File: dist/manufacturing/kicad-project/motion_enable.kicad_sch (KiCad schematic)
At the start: 16 parts, among them Q14 MMBT5551LT1G, Q15 MMBT5551LT1G, U10 SN74LVC1G08DBVR, U11 SN74LVC1G08DBVR, U8 74LVC1G157GW,125, U9 74LVC1G157GW,125

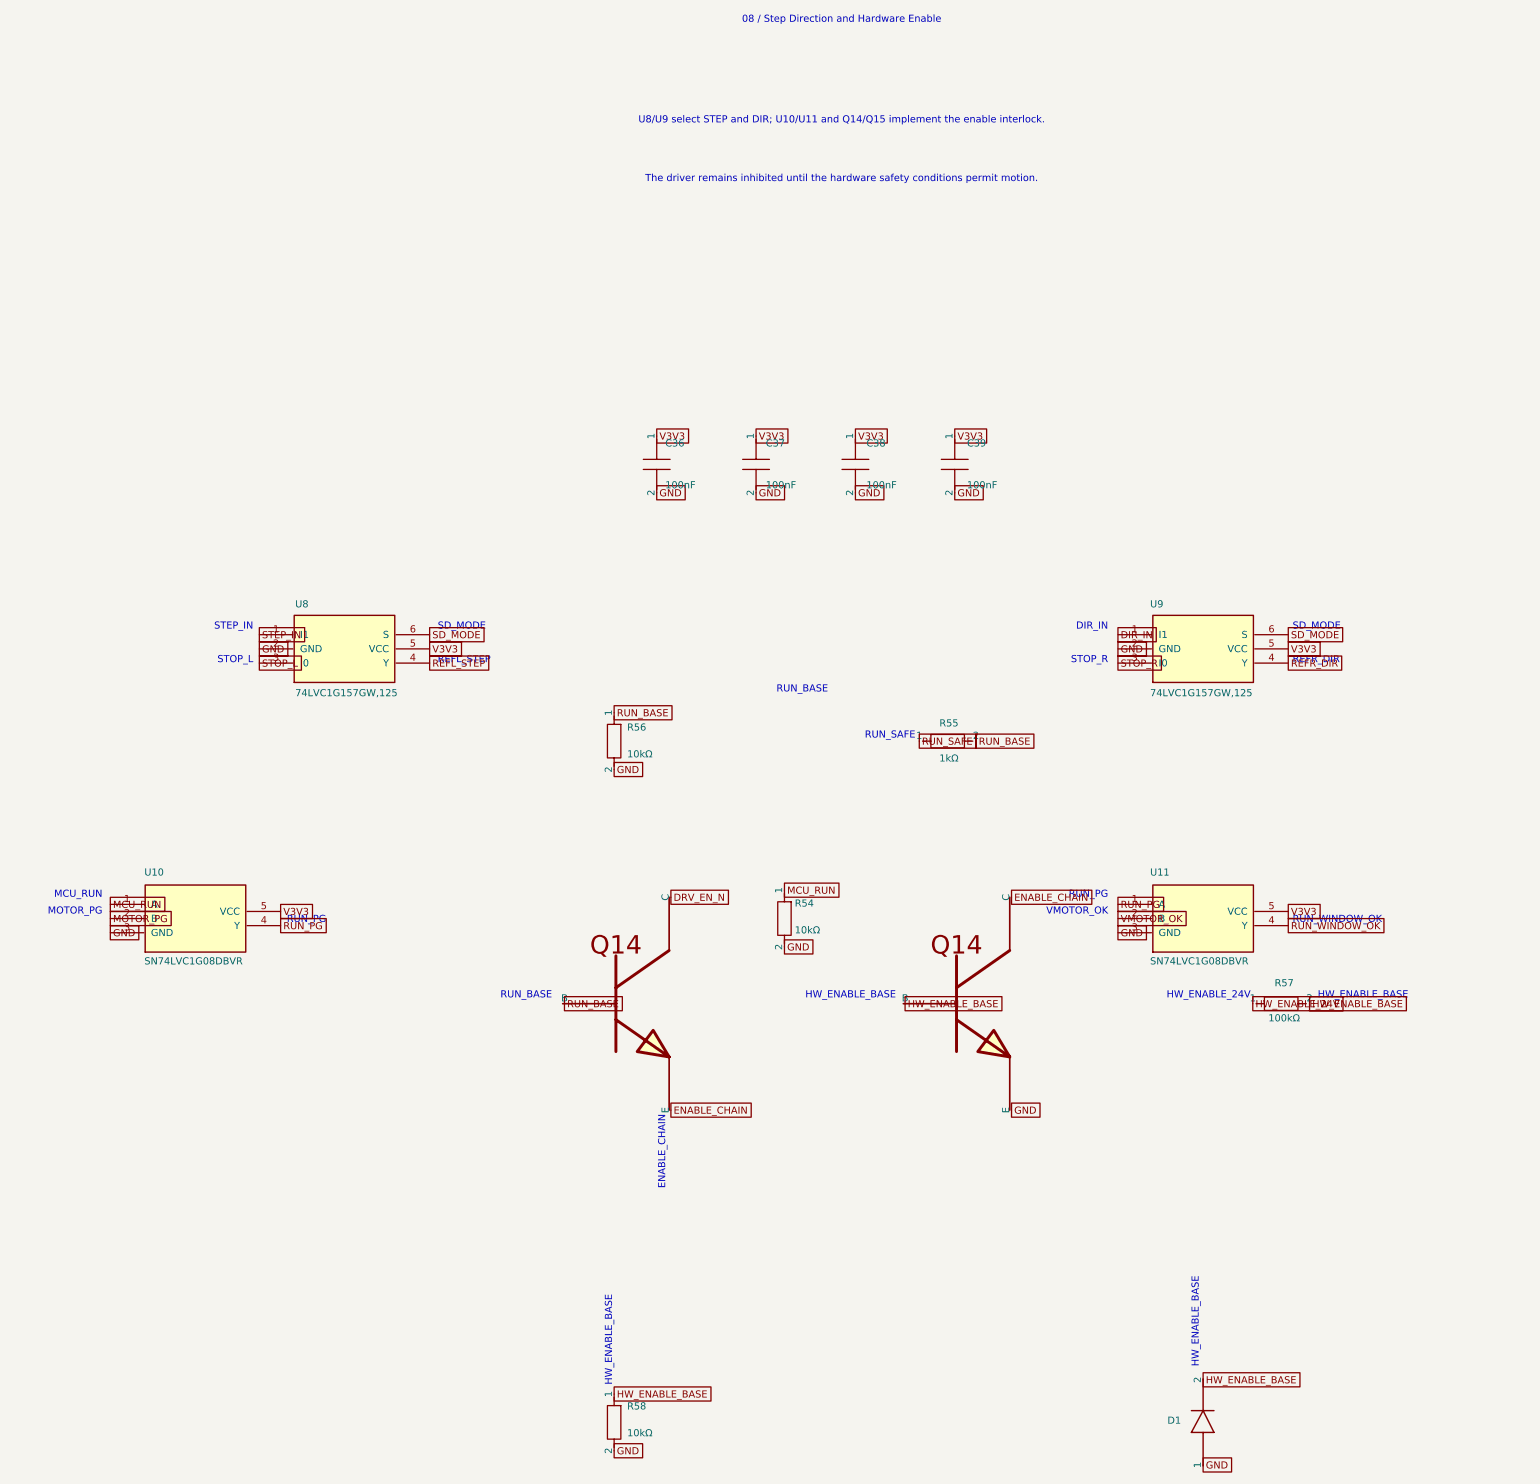
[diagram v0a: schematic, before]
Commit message: Implement motor harness and mounting; remove unsupported interfaces
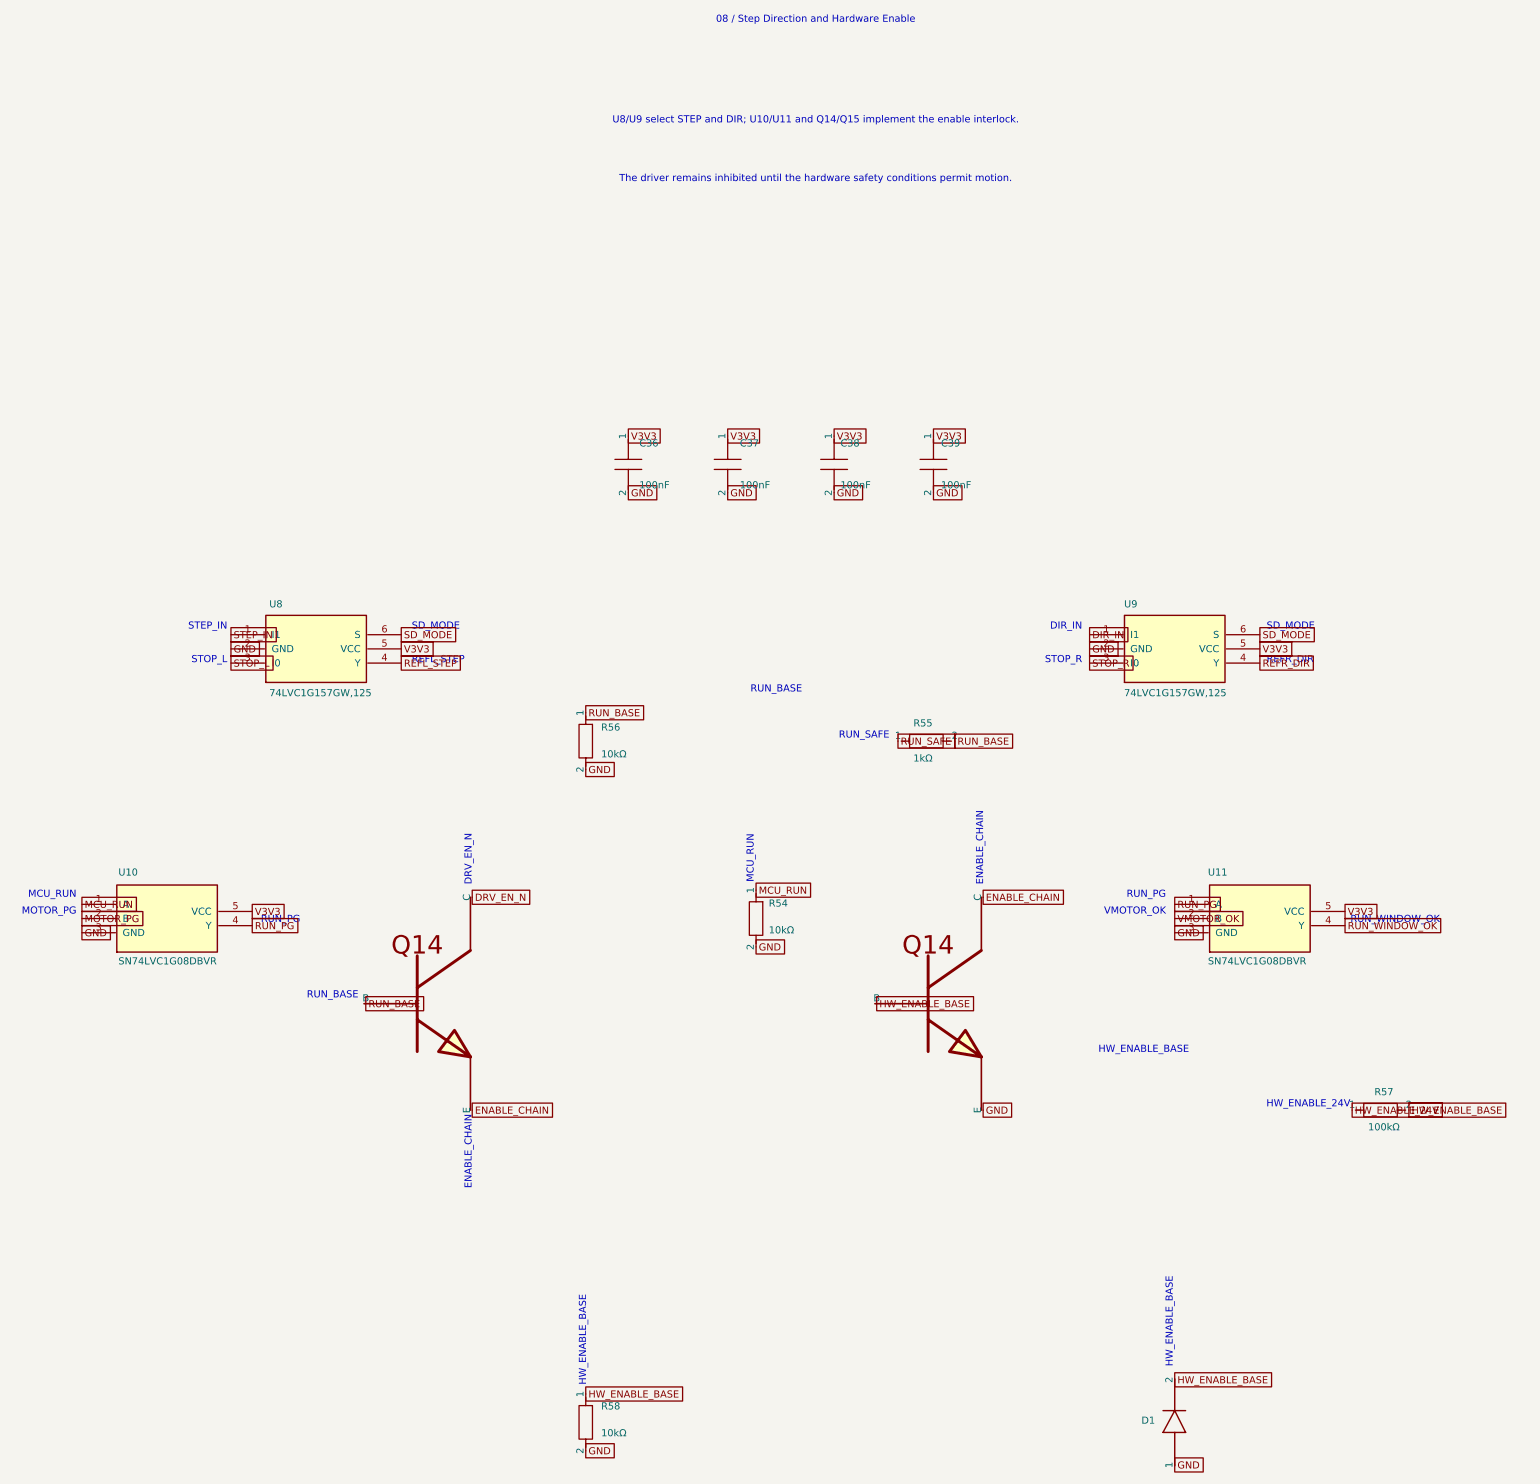
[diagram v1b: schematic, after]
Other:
- note added: "DRV_EN_N"

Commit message: Replace J7 with onboard control and simplify motor assembly
Add local START/STOP and fail-closed motion firmware, remove unsupported external command circuitry and mounting hardware, and preserve the four PCB holes and braking protection.

Refresh native PCB routing, manufacturing files, assembly previews, and build evidence. Local source/site builds and 66 regression tests pass; sourcing, placement review, and hardware qualification remain open.
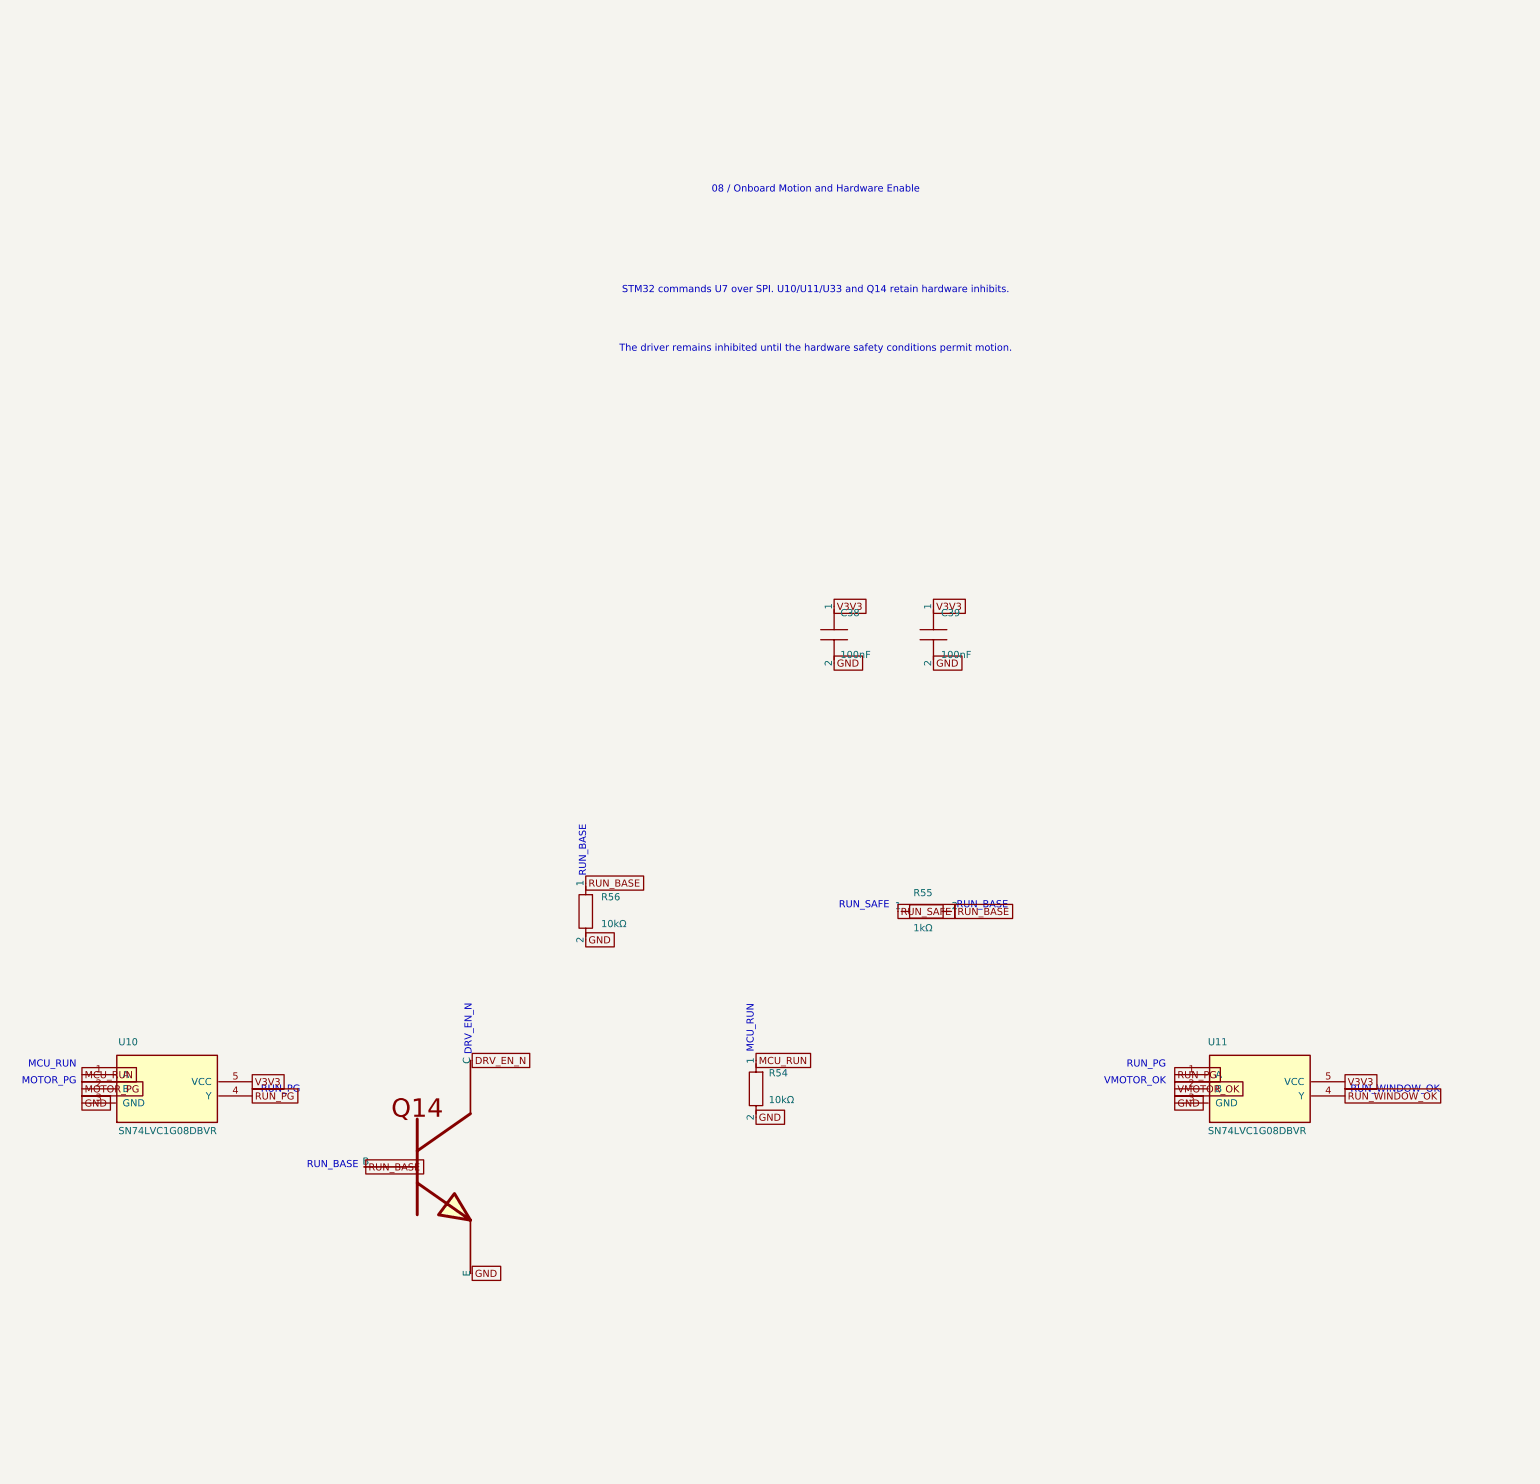
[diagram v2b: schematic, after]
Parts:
- removed C36, C37: 100nF, capacitor_cap0603, symbol Device:capacitor_down
- removed D1: D, BAV21W-7-F, symbol Device:diode_up
- removed Q15: MMBT5551LT1G, MMBT5551LT1G, symbol Custom:MMBT5551LT1G
- removed R57: 100kΩ, resistor_res0603, symbol Device:boxresistor_right
- removed R58: 10kΩ, resistor_res0603, symbol Device:boxresistor_down
- removed U8, U9: 74LVC1G157GW,125, 74LVC1G157GW_125, symbol Device:U_74LVC1G157GW_125
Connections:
- net ENABLE_CHAIN is gone; now on net GND: Q14.2 (E)
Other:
- note added: "08 / Onboard Motion and Hardware Enable"
- note added: "STM32 commands U7 over SPI. U10/U11/U33 and Q14 retain hardware inhibits."
- note removed: "08 / Step Direction and Hardware Enable"
- note removed: "DIR_IN"
- note removed: "ENABLE_CHAIN"
- note removed: "HW_ENABLE_24V"
- note removed: "HW_ENABLE_BASE"
- note removed: "REFL_STEP"
- note removed: "REFR_DIR"
- note removed: "SD_MODE"
- note removed: "STEP_IN"
- note removed: "STOP_L"
- note removed: "STOP_R"
- note removed: "U8/U9 select STEP and DIR; U10/U11 and Q14/Q15 implement the enable interlock."
